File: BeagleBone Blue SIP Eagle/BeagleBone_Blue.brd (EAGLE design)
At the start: 86.4 x 54.6 mm, 281 parts, among them M1 JST_ZH_2, M2 JST_ZH_2, M3 JST_ZH_2, M4 JST_ZH_2, P10 SCHA5B0200, Q3 MOSFET-N, U1 TPD4S012_DRY_6, U4 TPD4S012_DRY_6, U5 24LC_32AT-I/OT, U6 SN74LVC1G07_DCK_5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

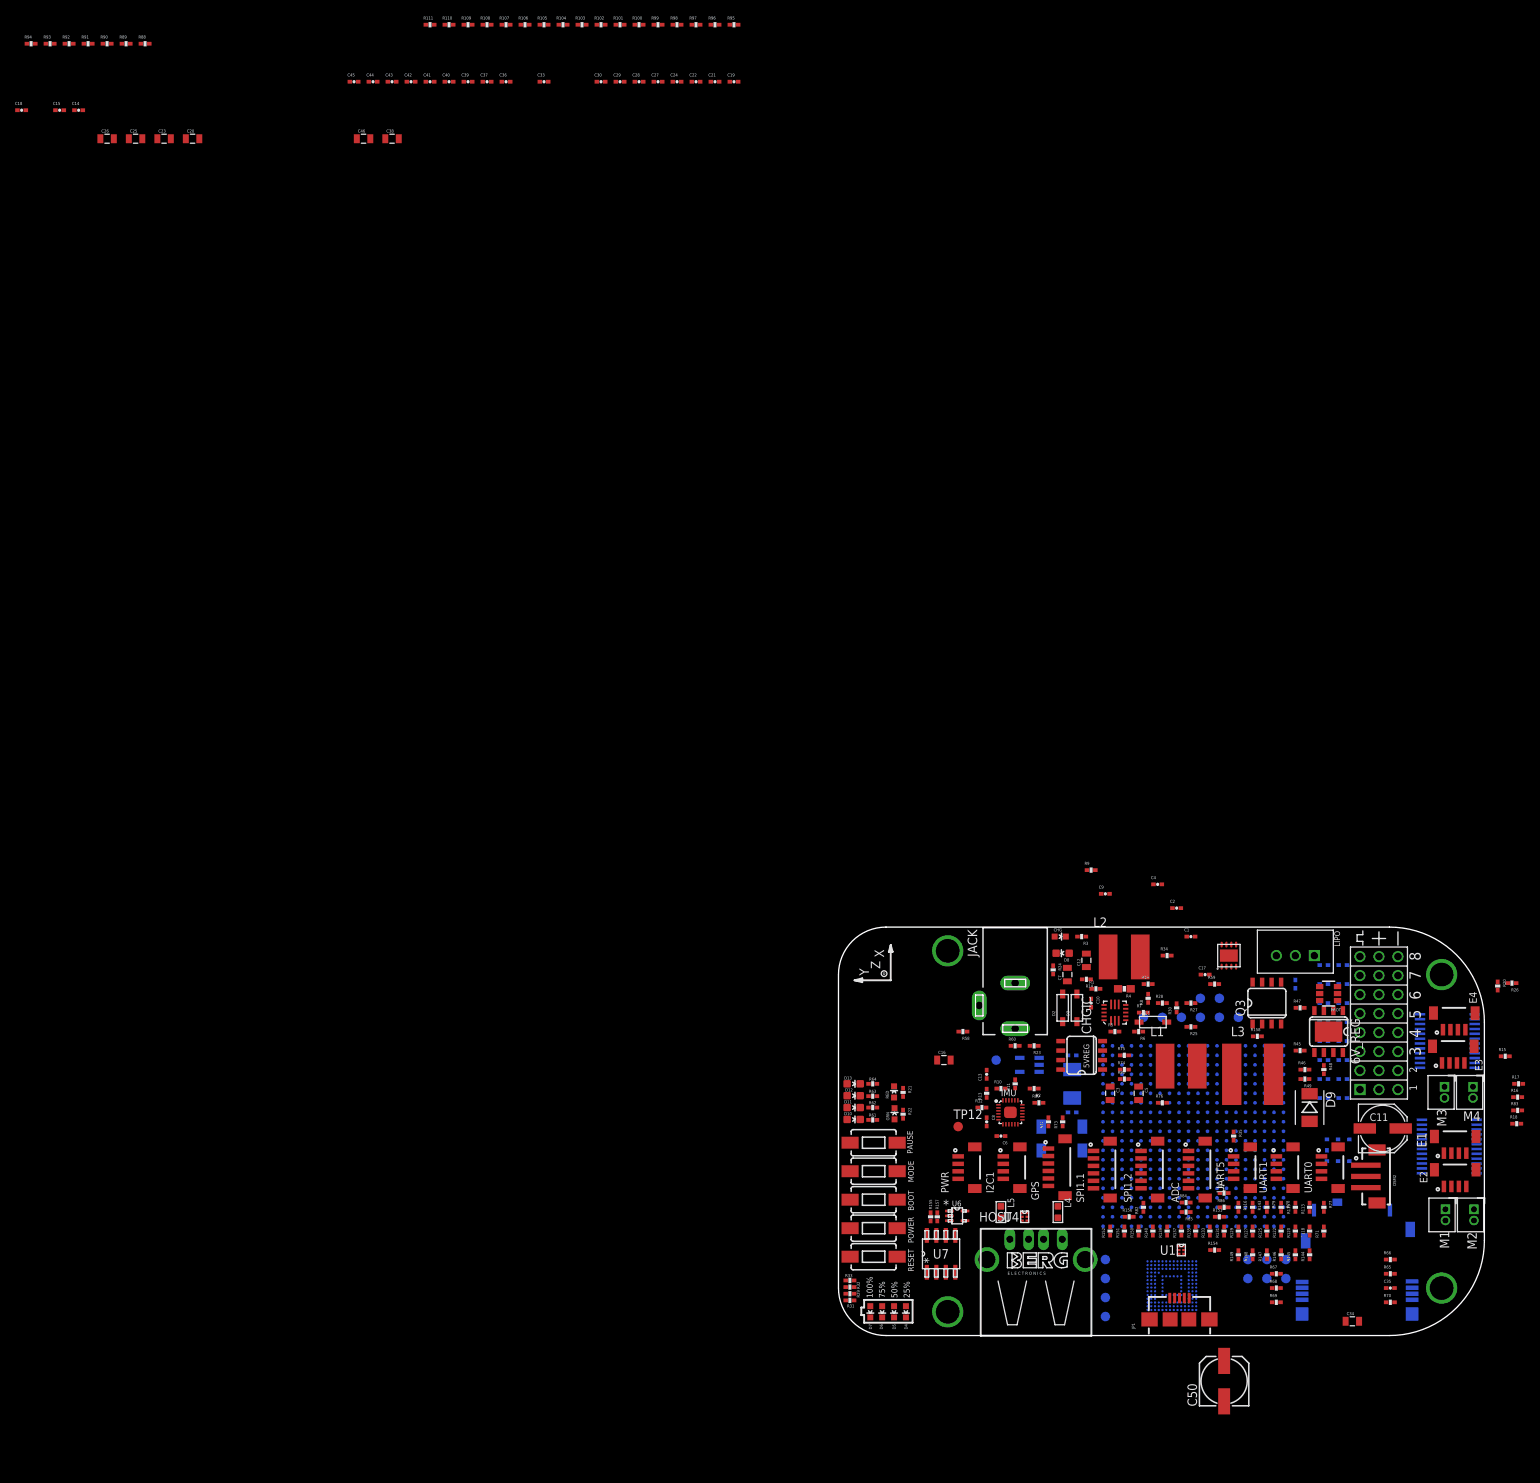
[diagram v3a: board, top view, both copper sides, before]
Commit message: new connector placement and screenshot
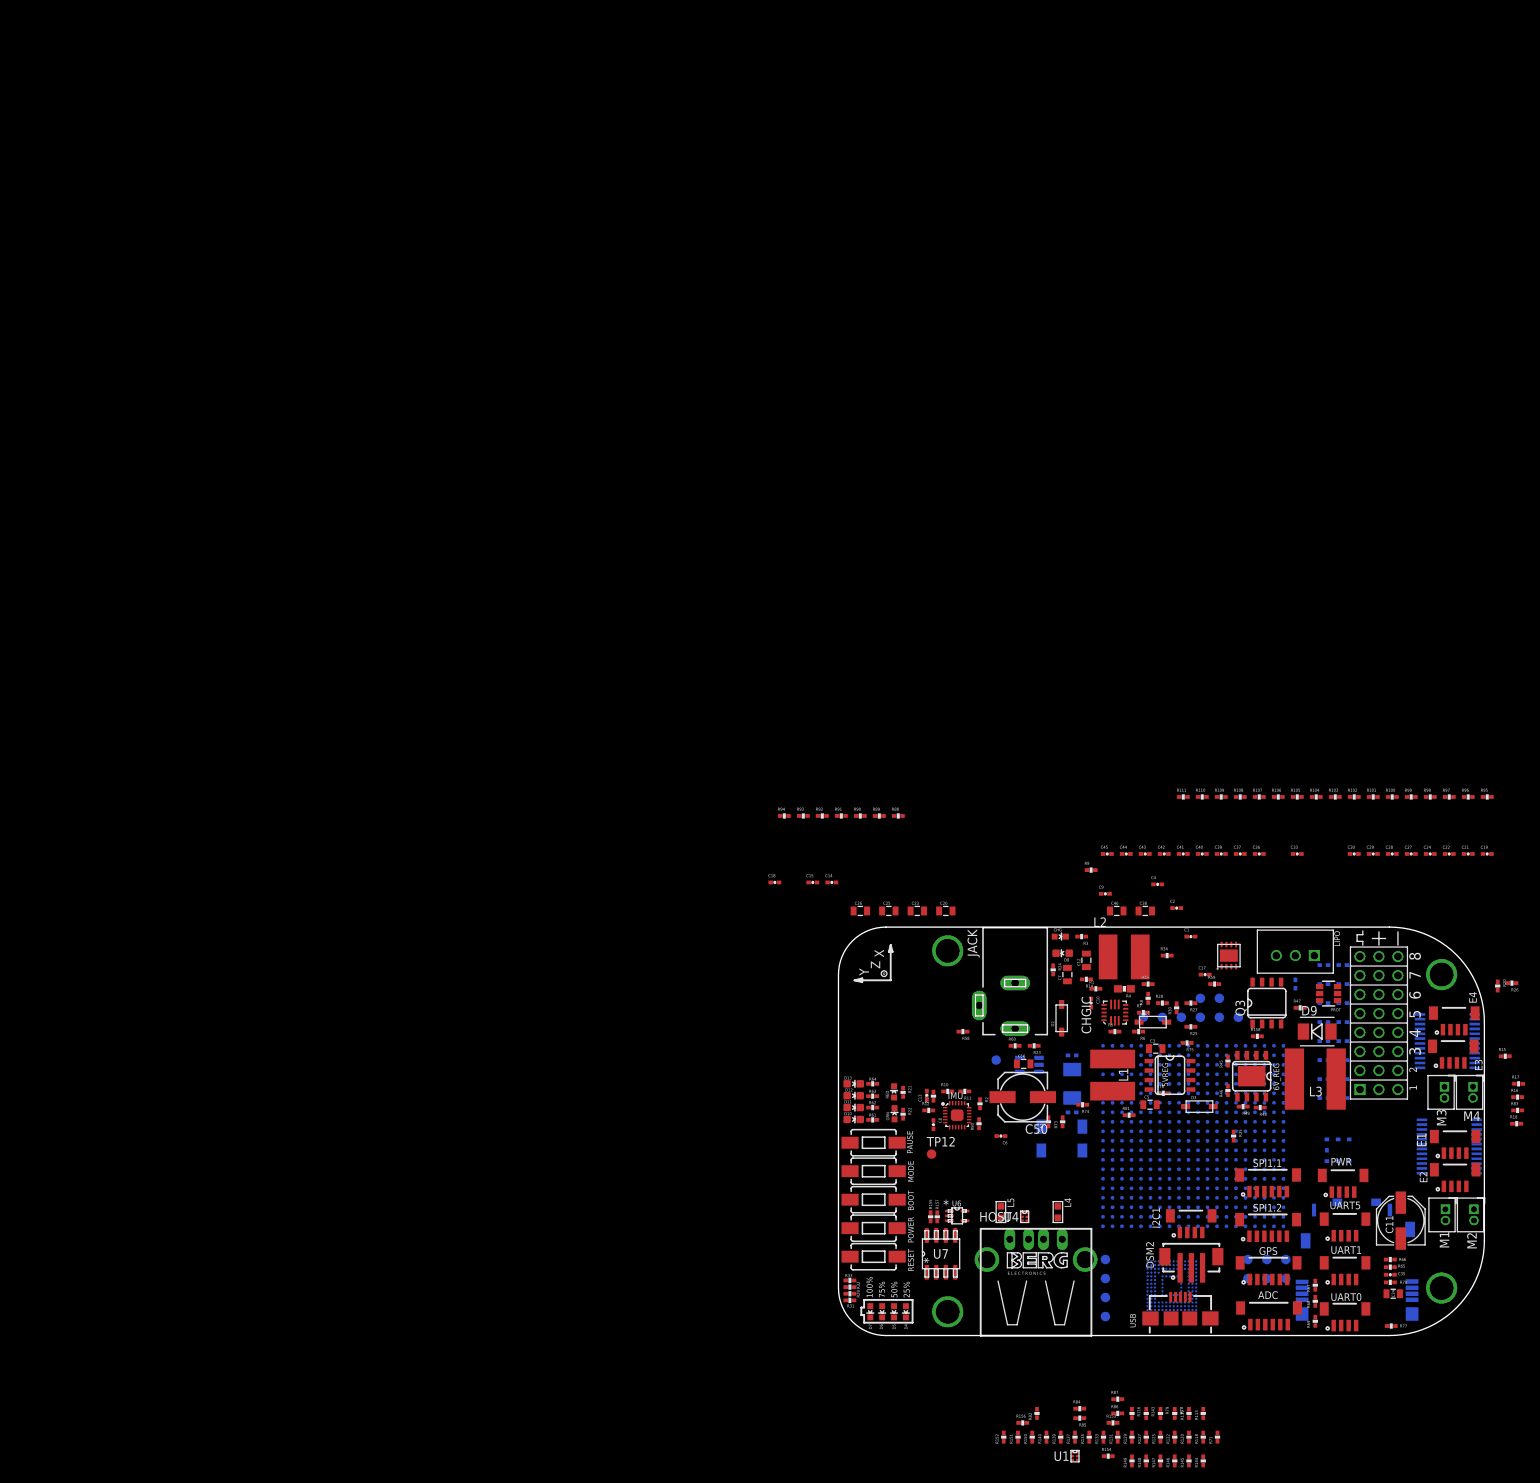
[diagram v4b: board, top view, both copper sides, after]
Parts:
- removed JP1: (no value), Strawson_Eagle_Lib:USB-AB-MICRO-SMD
- added USB: (no value), Strawson_Eagle_Lib:USB-AB-MICRO-SMD
- moved C20 144.2 mm to (14.4, 2.16)
- moved C23 144.2 mm to (10.5, 2.16)
- moved C25 144.2 mm to (6.73, 2.16)
- moved C26 144.2 mm to (2.92, 2.16)
- moved C29 144.2 mm to (71.5, 9.78)
- moved C36 144.2 mm to (56.3, 9.78)
- moved C38 144.2 mm to (41.0, 2.16)
- moved C46 144.2 mm to (37.2, 2.16)
- moved R101 144.2 mm to (71.5, 17.4)
- moved R103 144.2 mm to (66.4, 17.4)
- moved R107 144.2 mm to (56.3, 17.4)
- moved R90 144.2 mm to (2.92, 14.9)
- moved C14 144.2 mm to (-0.89, 5.97)
- moved C15 144.2 mm to (-3.43, 5.97)
- moved C18 144.2 mm to (-8.51, 5.97)
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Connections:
- net GND: now also USB.GND, USB.SHIELD1, USB.SHIELD2, USB.SHIELD3, USB.SHIELD4; no longer JP1.GND, JP1.SHIELD1, JP1.SHIELD2, JP1.SHIELD3, JP1.SHIELD4
- net N$117: now also USB.D+; no longer JP1.D+
- net N$118: now also USB.D-; no longer JP1.D-
- net N$119: now also USB.ID; no longer JP1.ID
- net USB0_VBUS: now also USB.VBUS; no longer JP1.VBUS

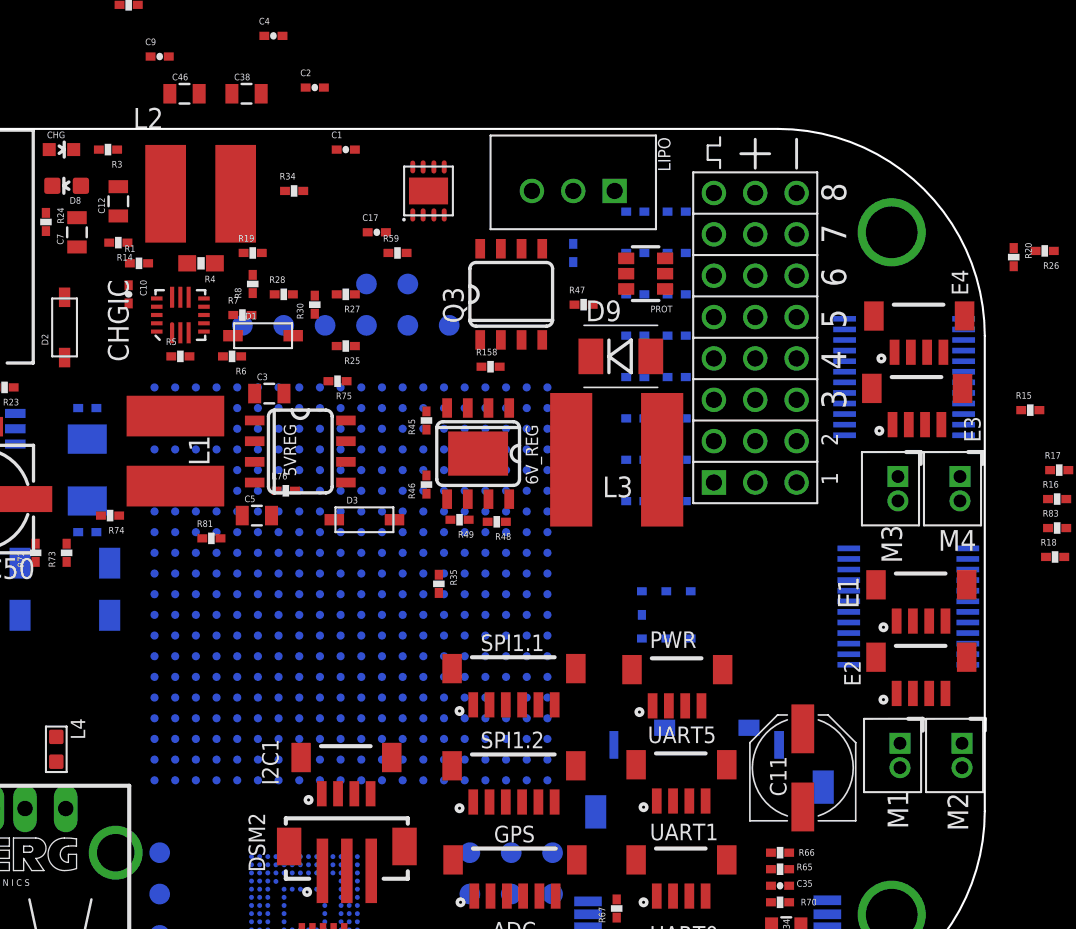
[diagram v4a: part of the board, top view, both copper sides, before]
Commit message: shuffle charging & protection circuit
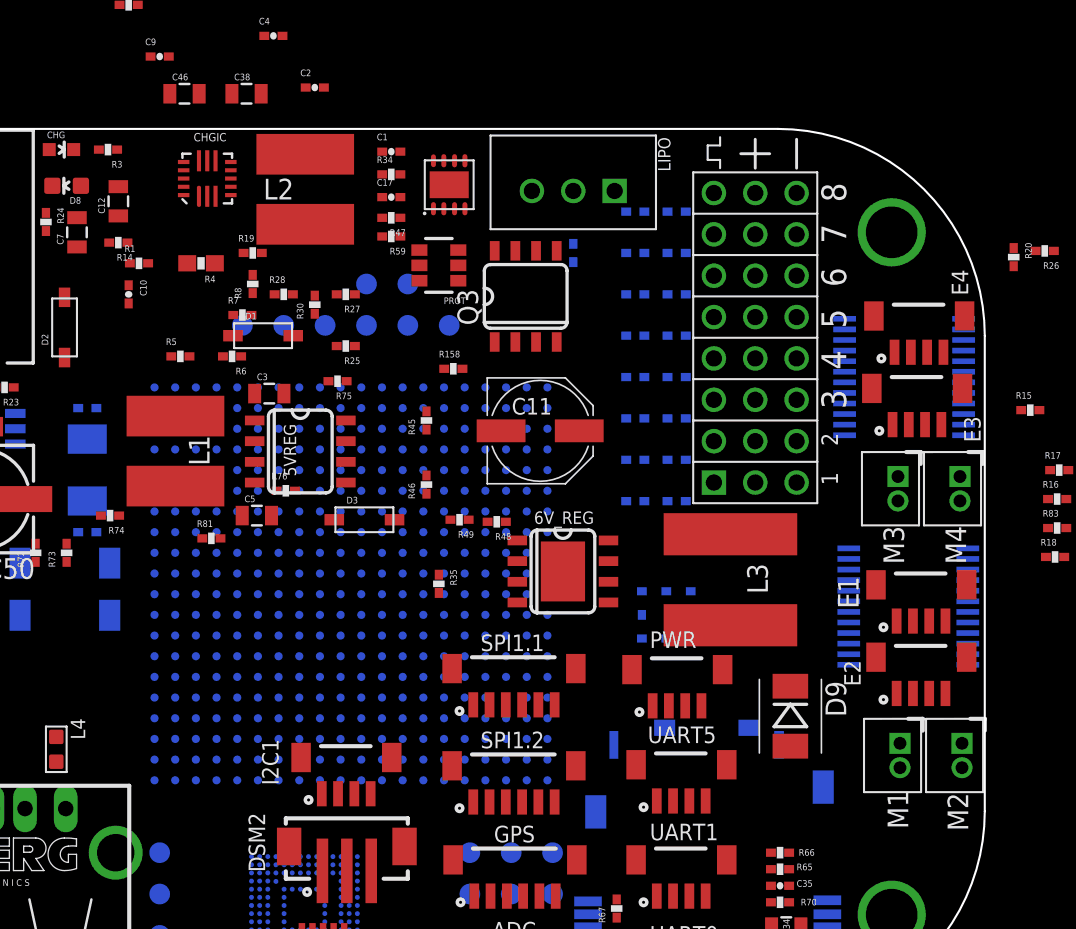
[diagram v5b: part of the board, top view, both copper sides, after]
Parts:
- moved C11 26.2 mm to (59.1, -18.5), turned to 0 degrees
- moved D9 24.4 mm to (74.4, -36.1), turned to 270 degrees
- moved R47 13.0 mm to (49.9, -5.46), turned to 180 degrees
- moved PROT 12.7 mm to (52.8, -8.38)
- moved L3 10.2 mm to (70.7, -27.7), turned to 270 degrees
- moved 6V_REG 8.92 mm to (60.5, -27.2), turned to 270 degrees
- moved CHGIC 8.54 mm to (38.6, -3.05)
- moved L2 6.22 mm to (44.5, -3.68), turned to 90 degrees
- moved R34 6.05 mm to (49.9, -2.79)
- moved C1 2.80 mm to (49.9, -1.40)
- moved C17 2.33 mm to (49.9, -4.19)
- moved R158 2.29 mm to (53.7, -14.7)
- moved BAL 1.33 mm to (53.5, -3.43)
- moved R59 1.09 mm to (49.9, -6.60), turned to 180 degrees
- moved Q3 0.90 mm to (58.2, -10.3)
